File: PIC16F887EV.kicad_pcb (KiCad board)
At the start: 2 copper layers, 100 x 100 mm, 89 parts, among them J1 Conn_01x05_Socket, P1 USB_C_Plug_USB2.0, Q1 2N3904, Q2 2N3904, Q3 2N3904, Q5 2N3904, SW1 SW_Push, SW10 SW_Push, SW11 SW_Push, SW12 SW_Push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

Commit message: Logo
Logo Taller Colaborativo de Electronica + Nombre de placa
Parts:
- added TCdE FCEFYN: Logo, Taller:Logo, F.Cu at (108.0, 61.0)
- moved P1 20.8 mm to (111.0, 83.0)
- moved CP2 3.68 mm to (104.8, 100.8)
- moved CP3 3.68 mm to (104.8, 92.9)
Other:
- board text added: "EV PIC16F887 v1.0"
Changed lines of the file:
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@@
     )
   )
+  (footprint "Taller:Logo" (layer "F.Cu")
+    (at 108 61)
+    (fp_text reference "TCdE FCEFYN" (at 0.3 7.6) (layer "F.SilkS") hide
+        (effects (font (size 1 1) (thickness 0.15)))
+    )
+    (fp_text value "Logo" (at 0 1) (layer "F.Fab")
+        (effects (font (size 1 1) (thickness 0.15)))
+    )
+    (fp_text user "FCEFyN" (at -5.2 12.2 unlocked) (layer "F.Cu")
+        (effects (font (size 2 2) (thickness 0.3)) (justify left bottom))
+    )
+    (fp_text user "TCdE" (at -4.2 9.1 unlocked) (layer "F.Cu")
+        (effects (font (size 2.5 2.5) (thickness 0.4)) (justify left bottom))
+    )
+    (fp_arc (start -3.1806 -2.7123) (mid 0.18748 -2.417618) (end 2.1267 0.3519)
+      (stroke (width 0.375) (type default)) (layer "F.Cu"))
+    (fp_arc (start -3.1344 -1.9226) (mid -0.187502 -1.768165) (end 1.4197 0.7067)
+      (stroke (width 0.375) (type default)) (layer "F.Cu"))
+    (fp_arc (start -2.2943 1.1837) (mid -1.939202 -5.591342) (end 3.9945 -2.3022)
+      (stroke (width 0.375) (type default)) (layer "F.Cu"))
+    (fp_arc (start -2.1747 0.3223) (mid -1.600349 -4.921577) (end 3.1903 -2.713)
+      (stroke (width 0.375) (type default)) (layer "F.Cu"))
+    (fp_arc (start -0.7587 4.1106) (mid -2.187537 1.04645) (end -0.7587 -2.0177)
+      (stroke (width 0.375) (type default)) (layer "F.Cu"))
+    (fp_arc (start -0.05016 3.7087) (mid -1.436651 1.018494) (end -0.0049 -1.6479)
+      (stroke (width 0.375) (type default)) (layer "F.Cu"))
+    (fp_arc (start 0.059 -2.5487) (mid 5.812442 1.04645) (end 0.059 4.6416)
+      (stroke (width 0.375) (type default)) (layer "F.Cu"))
+    (fp_arc (start 0.8082 -2.0445) (mid 5.062527 1.04645) (end 0.8082 4.1374)
+      (stroke (width 0.375) (type default)) (layer "F.Cu"))
+    (fp_arc (start 1.3542 1.7775) (mid -3.462005 3.846725) (end -3.9872 -1.3688)
+      (stroke (width 0.375) (type default)) (layer "F.Cu"))
+    (fp_arc (start 2.1723 1.3954) (mid -3.842915 4.493169) (end -4.0493 -2.2697)
+      (stroke (width 0.375) (type default)) (layer "F.Cu"))
+    (fp_arc (start 3.2376 -1.8096) (mid 1.624977 0.721693) (end -1.3735 0.8526)
+      (stroke (width 0.375) (type default)) (layer "F.Cu"))
+    (fp_arc (start 3.9392 -1.3983) (mid 1.99998 1.371218) (end -1.3681 1.6659)
+      (stroke (width 0.375) (type default)) (layer "F.Cu"))
+  )
   (footprint "Resistor_SMD:R_1206_3216Metric_Pad1.30x1.75mm_HandSolder" (layer "F.Cu")
     (at 27 75 180)
@@
   )
   (footprint "Capacitor_SMD:C_1206_3216Metric_Pad1.33x1.80mm_HandSolder" (layer "B.Cu")
-    (at 104.84 89.185 90)
+    (at 104.84 92.865 90)
     (descr "Capacitor SMD 1206 (3216 Metric), square (rectangular) end terminal, IPC_7351 nominal with elongated pad for handsoldering. (Body size source: IPC-SM-782 page 76, https://www.pcb-3d.com/wordpress/wp-content/uploads/ipc-sm-782a_amendment_1_and_2.pdf), generated with kicad-footprint-generator")
     (tags "capacitor handsolder")
@@
   )
   (footprint "Capacitor_SMD:C_1206_3216Metric_Pad1.33x1.80mm_HandSolder" (layer "B.Cu")
-    (at 104.84 97.1225 -90)
+    (at 104.84 100.8025 -90)
     (descr "Capacitor SMD 1206 (3216 Metric), square (rectangular) end terminal, IPC_7351 nominal with elongated pad for handsoldering. (Body size source: IPC-SM-782 page 76, https://www.pcb-3d.com/wordpress/wp-content/uploads/ipc-sm-782a_amendment_1_and_2.pdf), generated with kicad-footprint-generator")
     (tags "capacitor handsolder")
@@
   )
   (footprint "Connector_USB:USB_C_Receptacle_GCT_USB4105-xx-A_16P_TopMnt_Horizontal" (layer "B.Cu")
-    (at 110.49 62.23 -90)
+    (at 111 83 -90)
     (descr "USB 2.0 Type C Receptacle, GCT, 16P, top mounted, horizontal, 5A: https://gct.co/files/drawings/usb4105.pdf")
     (tags "USB C Type-C Receptacle SMD USB 2.0 16P 16C USB4105-15-A USB4105-15-A-060 USB4105-15-A-120 USB4105-GF-A USB4105-GF-A-060 USB4105-GF-A-120")
@@
   (gr_rect locked (start 15.24 15.24) (end 115.24 115.24)
     (stroke (width 0.25) (type solid)) (fill none) (layer "Edge.Cuts"))
+  (gr_text "EV PIC16F887 v1.0" (at 43 20) (layer "F.Cu")
+    (effects (font (size 3 3) (thickness 0.3) bold) (justify left bottom))
+  )
   (segment (start 34 54.45) (end 29.2225 54.45) (width 0.635) (layer "F.Cu") (net 1))
   (segment (start 18.44 51.9) (end 24.74 51.9) (width 0.635) (layer "F.Cu") (net 1))

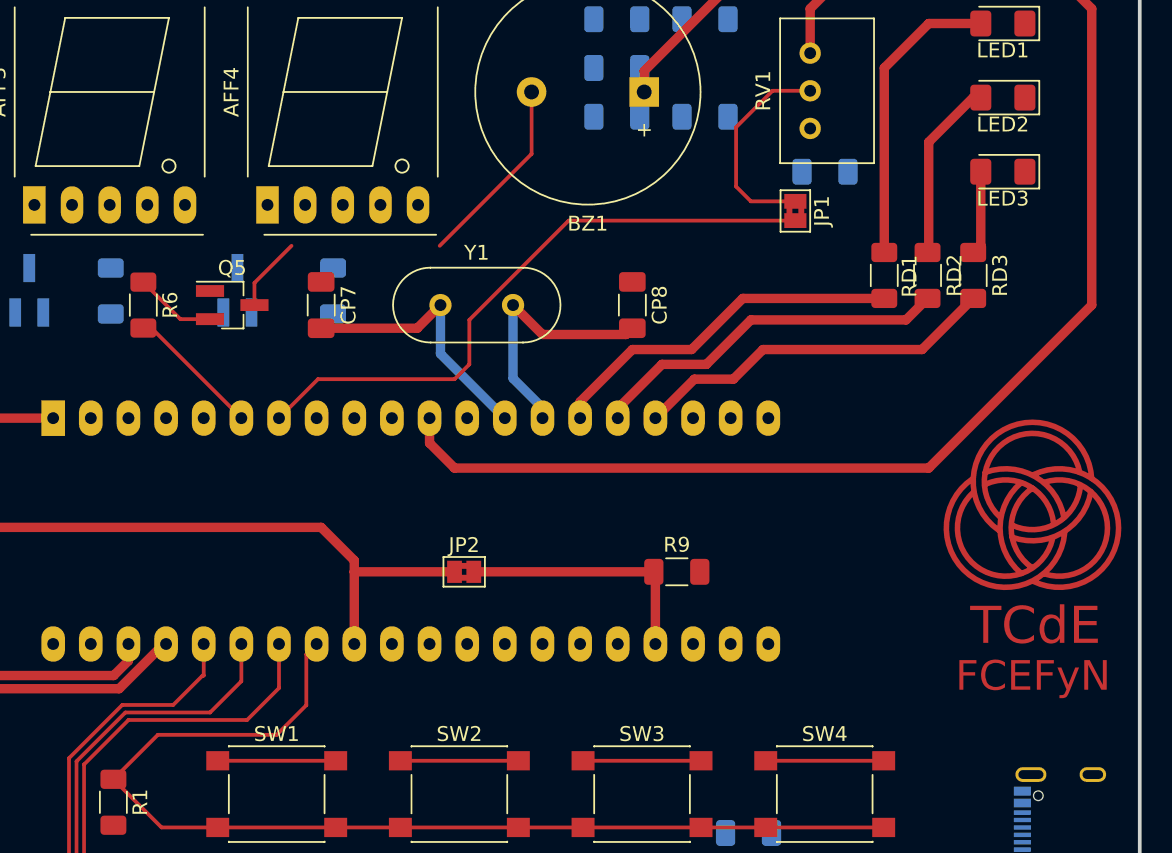
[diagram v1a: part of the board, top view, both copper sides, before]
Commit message: Jumpers modificados
tuve que cambiar la ubicación de uno porque estaba sobre el PIC
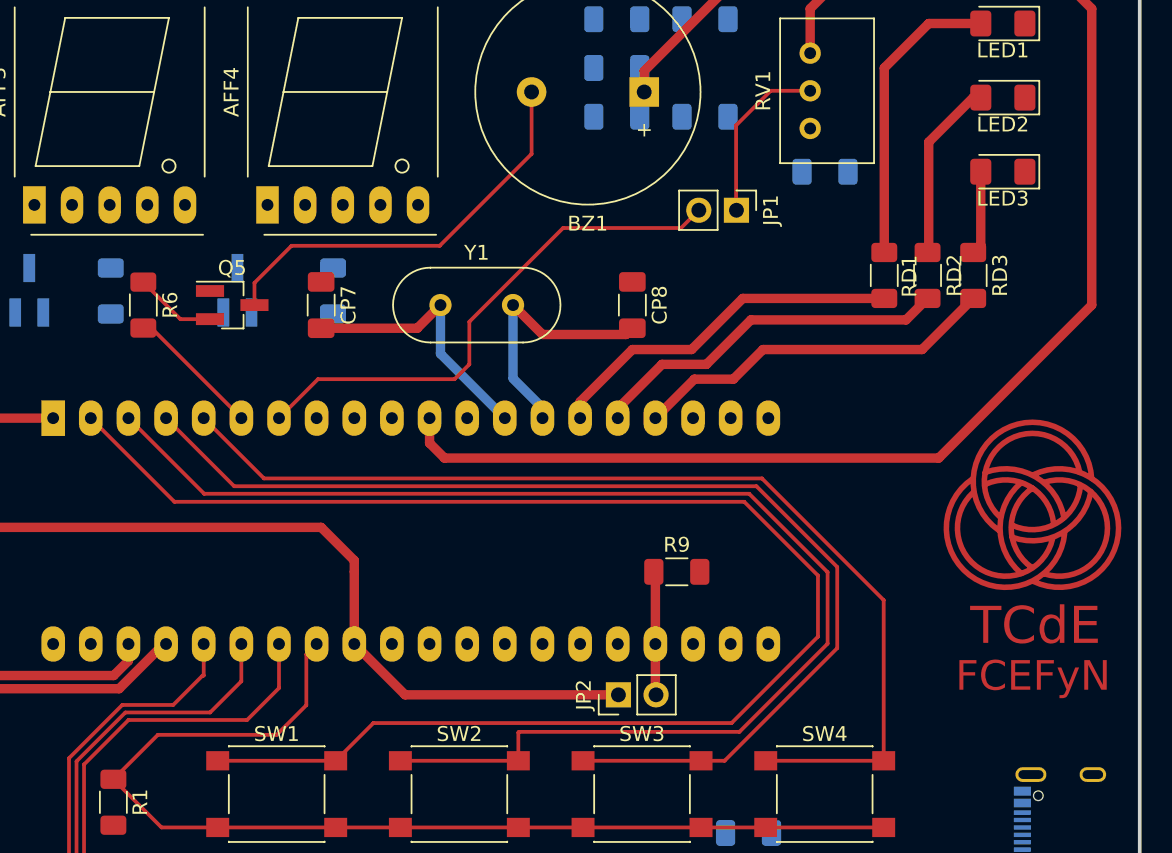
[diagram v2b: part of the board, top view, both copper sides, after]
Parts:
- JP1, JP2: footprint Jumper:SolderJumper-2_P1.3mm_Bridged2Bar_Pad1.0x1.5mm -> Connector_PinHeader_2.54mm:PinHeader_1x02_P2.54mm_Vertical
- moved JP2 13.3 mm to (80.1, 73.3), turned to 90 degrees
- moved JP1 3.98 mm to (88.0, 40.6)
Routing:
- net RA0: track 31.8 -> 125.4 mm
- net RA1: track 31.8 -> 113.4 mm
- net RA2: track 31.8 -> 99.1 mm
- net RA3: track 31.8 -> 93.8 mm
- net +5V: track 224.4 -> 236.3 mm
- net Net-(BZ1-+): track 18.0 -> 28.0 mm
- net Net-(JP2-B): track 17.2 -> 8.51 mm
- net RA5: track 42.6 -> 36.3 mm
- net Net-(JP1-A): track 14.4 -> 11.7 mm

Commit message: unc logo
agregue un mini logo de unc
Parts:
- added G***: LOGO, Libreria_Propia:unc_logo_4.3x6mm, F.Cu at (35.6, 109.2)

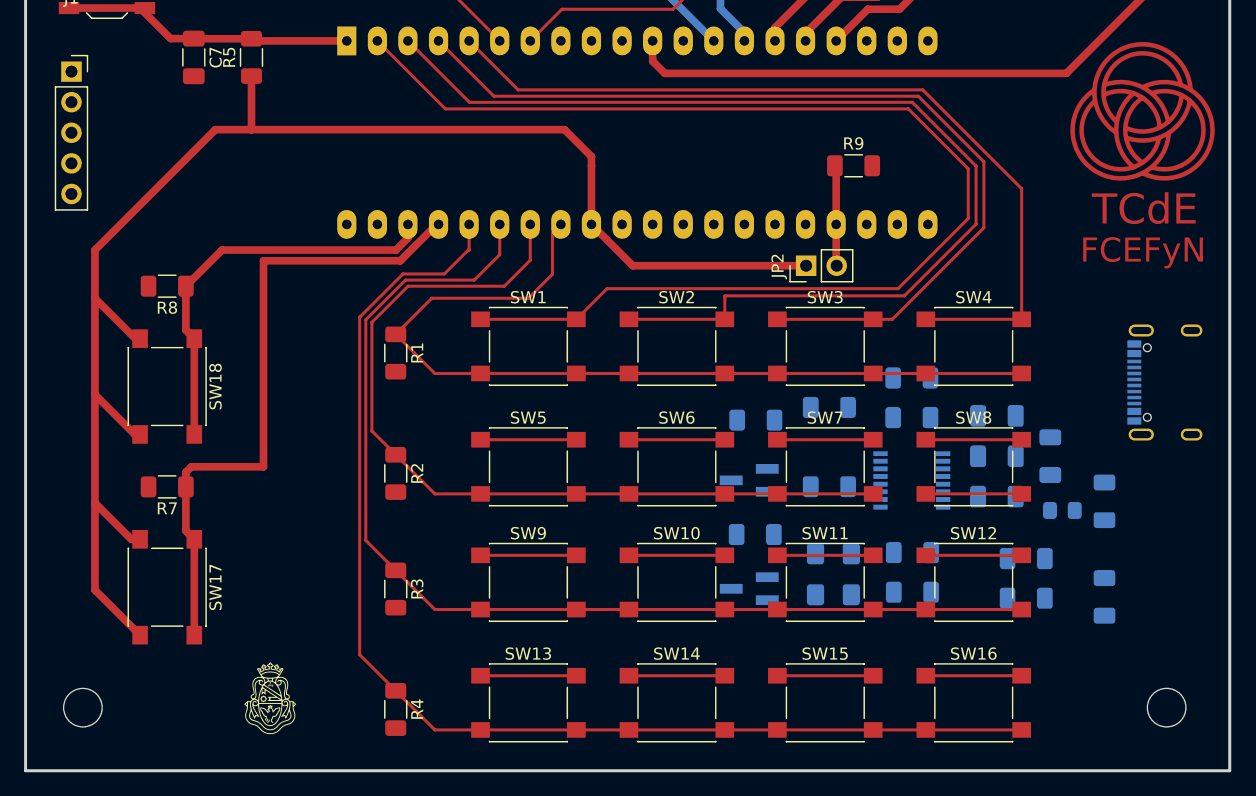
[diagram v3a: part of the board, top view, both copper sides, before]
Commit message: Texto y espaciado de teclado - jumper desplazado
* Agregue texto en el formato de 4x4, espesor 0.5 . --> Puede cambiarse, opte por ese formado por el teclado matricial comercial.
* Moví el jumper ,ya que se encontraba muy cerca del teclado y podría ser incomodo presionar.
* Conexiones comunes como +5v o GND en el PIC las desconecte para tener mas rutas en el ruteo (estas están conectadas internamente en el PIC)
* Conexión entre patas comunes en los pulsadores también las borre, sé que son comunes de a par, podría no tener sentido unirlas, ya que internamente lo están. (igual 
    es opcional, se puede volver a agregar)
* Opte por poner en un lateral las letras del teclado ya que no hay espacio suficiente (verticalmente) para que estén arriba o debajo de la tecla.
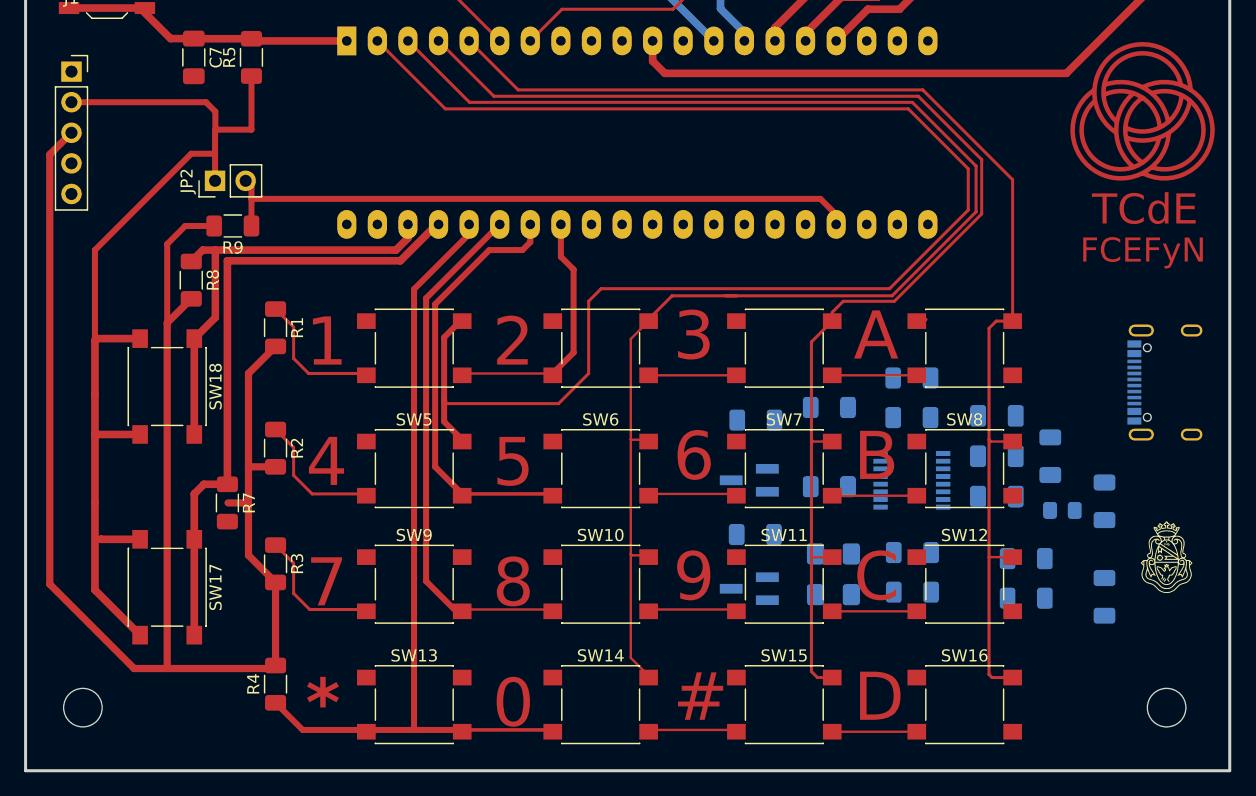
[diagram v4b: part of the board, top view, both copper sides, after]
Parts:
- moved G*** 75.4 mm to (110.0, 97.5)
- moved R9 51.8 mm to (32.5, 70.0), turned to 180 degrees
- moved JP2 49.6 mm to (31.0, 66.2)
- moved R3 10.2 mm to (36.0, 98.0)
- moved R4 10.2 mm to (36.0, 108.0), turned to 90 degrees
- moved R1 10.2 mm to (36.0, 78.5)
- moved R2 10.2 mm to (36.0, 88.5)
- moved SW1 9.48 mm to (47.5, 80.2)
- moved SW13 9.48 mm to (47.5, 109.8)
- moved SW5 9.48 mm to (47.5, 90.2)
- moved SW9 9.48 mm to (47.5, 99.8)
- moved SW10 6.33 mm to (63.0, 99.8)
- moved SW14 6.33 mm to (63.0, 109.8)
- moved SW2 6.33 mm to (63.0, 80.2)
- moved SW6 6.33 mm to (63.0, 90.2)
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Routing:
- net GND: track 0.00 -> 135.0 mm
- net Net-(JP2-B): track 8.51 -> 54.5 mm
- net +5V: track 236.3 -> 194.3 mm
- net RB0: track 72.8 -> 46.6 mm
- net RB2: track 91.0 -> 69.6 mm
- net RB1: track 79.0 -> 62.2 mm
- net RB3: track 99.1 -> 82.3 mm
- net RA1: track 113.4 -> 120.7 mm
- net RA2: track 99.1 -> 105.5 mm
- net RA3: track 93.8 -> 98.8 mm
- net RA0: track 125.4 -> 121.9 mm
- net RB5: track 33.8 -> 36.0 mm
- net RB4: track 53.3 -> 52.2 mm
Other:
- board text added: "#"
- board text added: "*"
- board text added: "0"
- board text added: "1"
- board text added: "2"
- board text added: "3"
- board text added: "4"
- board text added: "5"
- board text added: "6"
- board text added: "7"
- board text added: "8"
- board text added: "9"
- board text added: "A"
- board text added: "B"
- board text added: "C"
- board text added: "D"
